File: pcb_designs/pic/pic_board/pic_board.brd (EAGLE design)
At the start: 110.5 x 77.1 mm, 22 parts, among them IC1 PIC16f877a, IC2 7805TV

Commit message: modify
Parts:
- added R3: 10K, rcl:0204/7
- added SL1, SL2: 4 pin, con-amp-quick:04P
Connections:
- new net N$39: IC1.1, R3.2
- net N$33: now also R3.1, SL2.1, SL2.2, SL2.3, SL2.4; no longer IC1.1
- net N$35: now also SL1.1, SL1.2, SL1.3, SL1.4
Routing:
- net N$33: track 127.0 -> 146.0 mm
- net N$35: track 272.8 -> 288.1 mm
- net N$39: track 0.00 -> 6.88 mm
- net N$1: track 27.0 -> 29.2 mm
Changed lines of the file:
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@@
 <layer number="18" name="Vias" color="2" fill="1" visible="yes" active="yes"/>
 <layer number="19" name="Unrouted" color="6" fill="1" visible="yes" active="yes"/>
-<layer number="20" name="Dimension" color="15" fill="1" visible="yes" active="yes"/>
+<layer number="20" name="Dimension" color="15" fill="1" visible="no" active="yes"/>
 <layer number="21" name="tPlace" color="7" fill="1" visible="no" active="yes"/>
 <layer number="22" name="bPlace" color="7" fill="1" visible="no" active="yes"/>
@@
 <rectangle x1="0" y1="-1.27" x2="7.62" y2="5.08" layer="16"/>
 <rectangle x1="-8.89" y1="-3.81" x2="-1.27" y2="6.35" layer="16"/>
-<rectangle x1="48.26" y1="46.99" x2="64.77" y2="54.61" layer="16"/>
-<rectangle x1="27.94" y1="41.91" x2="39.37" y2="49.53" layer="16"/>
 <rectangle x1="11.43" y1="-7.62" x2="25.4" y2="5.08" layer="16"/>
 <text x="-15.24" y="30.48" size="2.286" layer="1" rot="R270">PIC BOARD</text>
@@
 <attribute name="OC_FARNELL" value="unknown" x="72.39" y="0" size="1.778" layer="27" rot="R270" display="off"/>
 </element>
+<element name="SL1" library="con-amp-quick" package="04P" value="4 pin" x="58.42" y="49.53">
+<attribute name="OC_NEWARK" value="unknown" x="58.42" y="49.53" size="1.778" layer="27" display="off"/>
+<attribute name="MPN" value="" x="58.42" y="49.53" size="1.778" layer="27" display="off"/>
+<attribute name="MF" value="" x="58.42" y="49.53" size="1.778" layer="27" display="off"/>
+<attribute name="OC_FARNELL" value="unknown" x="58.42" y="49.53" size="1.778" layer="27" display="off"/>
+</element>
+<element name="SL2" library="con-amp-quick" package="04P" value="4 pin" x="33.02" y="48.26" rot="R180">
+<attribute name="OC_NEWARK" value="unknown" x="33.02" y="48.26" size="1.778" layer="27" rot="R180" display="off"/>
+<attribute name="MPN" value="" x="33.02" y="48.26" size="1.778" layer="27" rot="R180" display="off"/>
+<attribute name="MF" value="" x="33.02" y="48.26" size="1.778" layer="27" rot="R180" display="off"/>
+<attribute name="OC_FARNELL" value="unknown" x="33.02" y="48.26" size="1.778" layer="27" rot="R180" display="off"/>
+</element>
+<element name="R3" library="rcl" package="0204/7" value="10K" x="31.75" y="43.18"/>
 </elements>
 <signals>
@@
 <contactref element="C2" pad="1"/>
 <wire x1="16.51" y1="15.24" x2="24.13" y2="15.24" width="1.27" layer="16"/>
-<wire x1="27.94" y1="11.43" x2="41.91" y2="11.43" width="1.27" layer="16"/>
-<wire x1="24.13" y1="15.24" x2="27.94" y2="11.43" width="1.27" layer="16"/>
+<wire x1="25.4" y1="11.43" x2="41.91" y2="11.43" width="1.27" layer="16"/>
+<wire x1="24.13" y1="15.24" x2="25.4" y2="15.24" width="1.27" layer="16"/>
+<wire x1="25.4" y1="15.24" x2="25.4" y2="11.43" width="1.27" layer="16"/>
 </signal>
 <signal name="N$2">
@@
 <contactref element="C6" pad="1"/>
 <contactref element="IC1" pad="32"/>
-<contactref element="IC1" pad="1"/>
 <contactref element="R2" pad="2"/>
 <contactref element="IC1" pad="11"/>
@@
 <wire x1="43.18" y1="59.69" x2="26.67" y2="59.69" width="1.27" layer="16"/>
 <wire x1="26.67" y1="59.69" x2="0" y2="59.69" width="1.27" layer="16"/>
-<wire x1="43.18" y1="41.91" x2="43.18" y2="57.15" width="1.27" layer="16"/>
+<wire x1="44.45" y1="48.26" x2="43.18" y2="48.26" width="1.27" layer="16"/>
+<wire x1="43.18" y1="48.26" x2="43.18" y2="57.15" width="1.27" layer="16"/>
 <wire x1="43.18" y1="57.15" x2="43.18" y2="59.69" width="1.27" layer="16"/>
 <wire x1="26.67" y1="59.69" x2="26.67" y2="55.88" width="1.27" layer="16"/>
 <wire x1="53.34" y1="57.15" x2="53.34" y2="58.42" width="1.27" layer="16"/>
 <wire x1="43.18" y1="57.15" x2="53.34" y2="57.15" width="1.27" layer="16"/>
-<wire x1="44.45" y1="41.91" x2="44.45" y2="16.51" width="1.27" layer="16"/>
-<wire x1="41.91" y1="41.91" x2="43.18" y2="41.91" width="1.27" layer="16"/>
-<wire x1="43.18" y1="41.91" x2="44.45" y2="41.91" width="1.27" layer="16"/>
+<wire x1="44.45" y1="48.26" x2="44.45" y2="16.51" width="1.27" layer="16"/>
+<contactref element="SL2" pad="1"/>
+<contactref element="SL2" pad="2"/>
+<contactref element="SL2" pad="3"/>
+<contactref element="SL2" pad="4"/>
+<wire x1="31.75" y1="48.26" x2="29.21" y2="48.26" width="1.27" layer="16"/>
+<wire x1="31.75" y1="48.26" x2="34.29" y2="48.26" width="1.27" layer="16"/>
+<wire x1="34.29" y1="48.26" x2="36.83" y2="48.26" width="1.27" layer="16"/>
+<wire x1="43.18" y1="48.26" x2="36.83" y2="48.26" width="1.27" layer="16"/>
+<contactref element="R3" pad="1"/>
+<wire x1="27.94" y1="48.26" x2="27.94" y2="43.18" width="1.27" layer="16"/>
+<wire x1="29.21" y1="48.26" x2="27.94" y2="48.26" width="1.27" layer="16"/>
 </signal>
 <signal name="N$35">
@@
 <wire x1="57.15" y1="19.05" x2="63.5" y2="19.05" width="1.27" layer="16"/>
 <wire x1="63.5" y1="19.05" x2="68.58" y2="19.05" width="1.27" layer="16"/>
-<wire x1="69.85" y1="44.45" x2="69.85" y2="58.42" width="1.27" layer="16"/>
+<wire x1="69.85" y1="44.45" x2="69.85" y2="49.53" width="1.27" layer="16"/>
+<wire x1="69.85" y1="49.53" x2="69.85" y2="58.42" width="1.27" layer="16"/>
 <wire x1="69.85" y1="58.42" x2="55.88" y2="58.42" width="1.27" layer="16"/>
 <wire x1="73.66" y1="44.45" x2="69.85" y2="44.45" width="1.27" layer="16"/>
@@
 <wire x1="27.94" y1="17.78" x2="27.94" y2="13.97" width="1.27" layer="16"/>
 <wire x1="13.97" y1="17.78" x2="27.94" y2="17.78" width="1.27" layer="16"/>
+<contactref element="SL1" pad="1"/>
+<contactref element="SL1" pad="2"/>
+<contactref element="SL1" pad="3"/>
+<contactref element="SL1" pad="4"/>
+<wire x1="57.15" y1="49.53" x2="54.61" y2="49.53" width="1.27" layer="16"/>
+<wire x1="57.15" y1="49.53" x2="59.69" y2="49.53" width="1.27" layer="16"/>
+<wire x1="59.69" y1="49.53" x2="62.23" y2="49.53" width="1.27" layer="16"/>
+<wire x1="69.85" y1="49.53" x2="62.23" y2="49.53" width="1.27" layer="16"/>
 </signal>
 <signal name="N$3">
@@
 <wire x1="72.39" y1="-6.35" x2="57.15" y2="-6.35" width="1.27" layer="16"/>
 </signal>
+<signal name="N$39">
+<contactref element="IC1" pad="1"/>
+<contactref element="R3" pad="2"/>
+<wire x1="36.83" y1="41.91" x2="35.56" y2="43.18" width="1.27" layer="16"/>
+<wire x1="41.91" y1="41.91" x2="36.83" y2="41.91" width="1.27" layer="16"/>
+</signal>
 </signals>

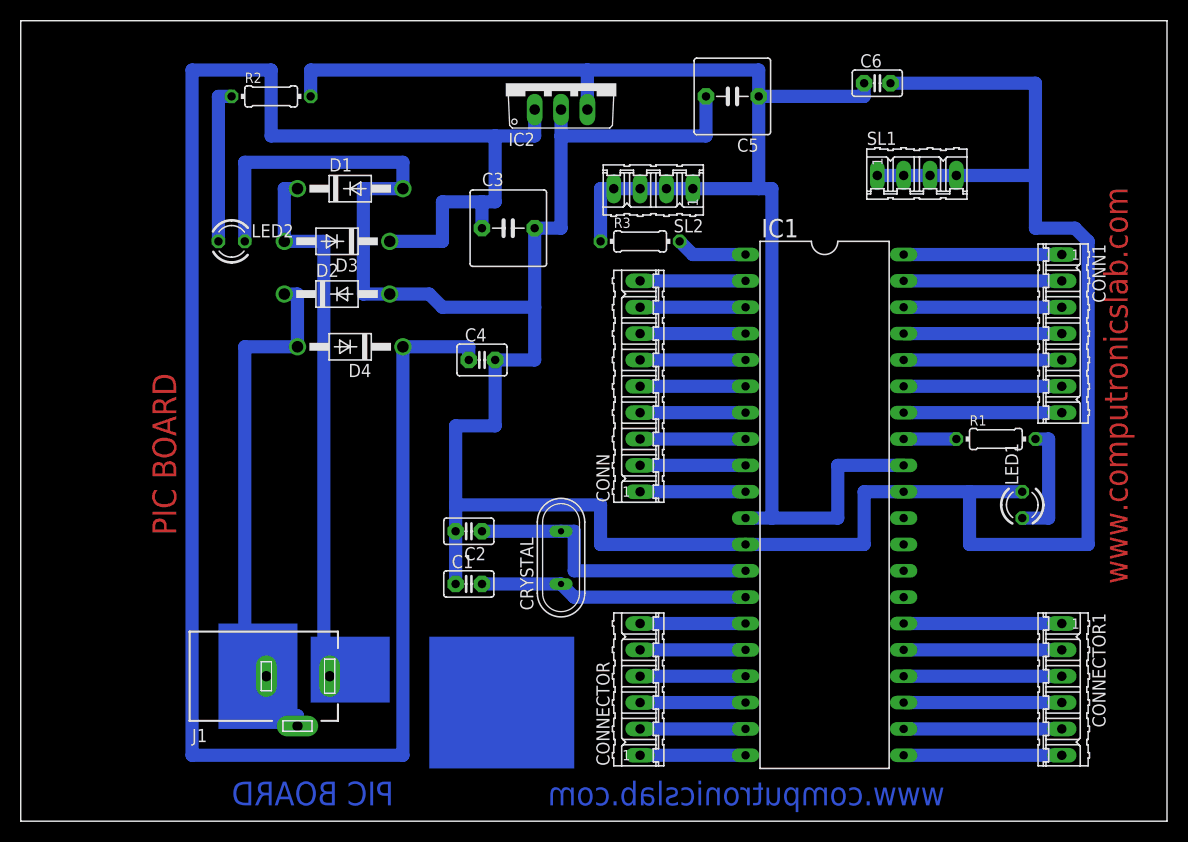
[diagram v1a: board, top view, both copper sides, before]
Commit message: ADD PIC WITH LCD
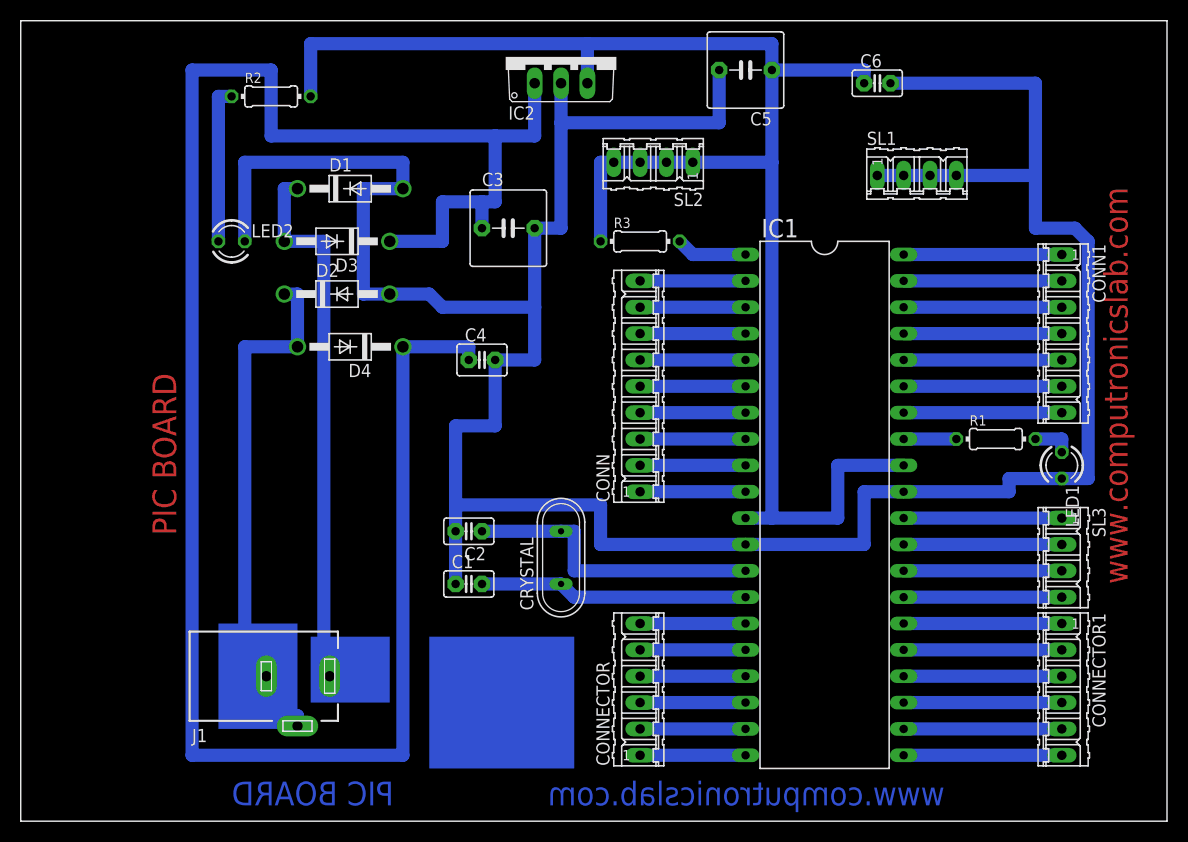
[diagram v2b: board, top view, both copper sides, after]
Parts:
- added SL3: 4 pin, con-amp-quick:04P
- moved LED1 5.39 mm to (72.4, 21.6), turned to 270 degrees
- moved C5 2.84 mm to (41.9, 59.7)
- moved IC2 2.54 mm to (24.1, 61.0)
- moved SL2 2.54 mm to (33.0, 50.8)
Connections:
- new net N$40: IC1.30, SL3.1
- new net N$41: IC1.29, SL3.2
- new net N$42: IC1.28, SL3.3
- new net N$43: IC1.27, SL3.4
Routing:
- net N$43: track 0.00 -> 15.2 mm
- net N$42: track 0.00 -> 15.2 mm
- net N$41: track 0.00 -> 15.2 mm
- net N$40: track 0.00 -> 15.2 mm
- net N$35: track 288.1 -> 277.9 mm
- net N$3: track 11.4 -> 3.81 mm
- net N$33: track 146.0 -> 153.7 mm
- net N$30: track 198.1 -> 200.7 mm
